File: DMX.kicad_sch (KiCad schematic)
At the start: 11 parts, among them J2 NC3FAAH, U2 CA-IS2092A

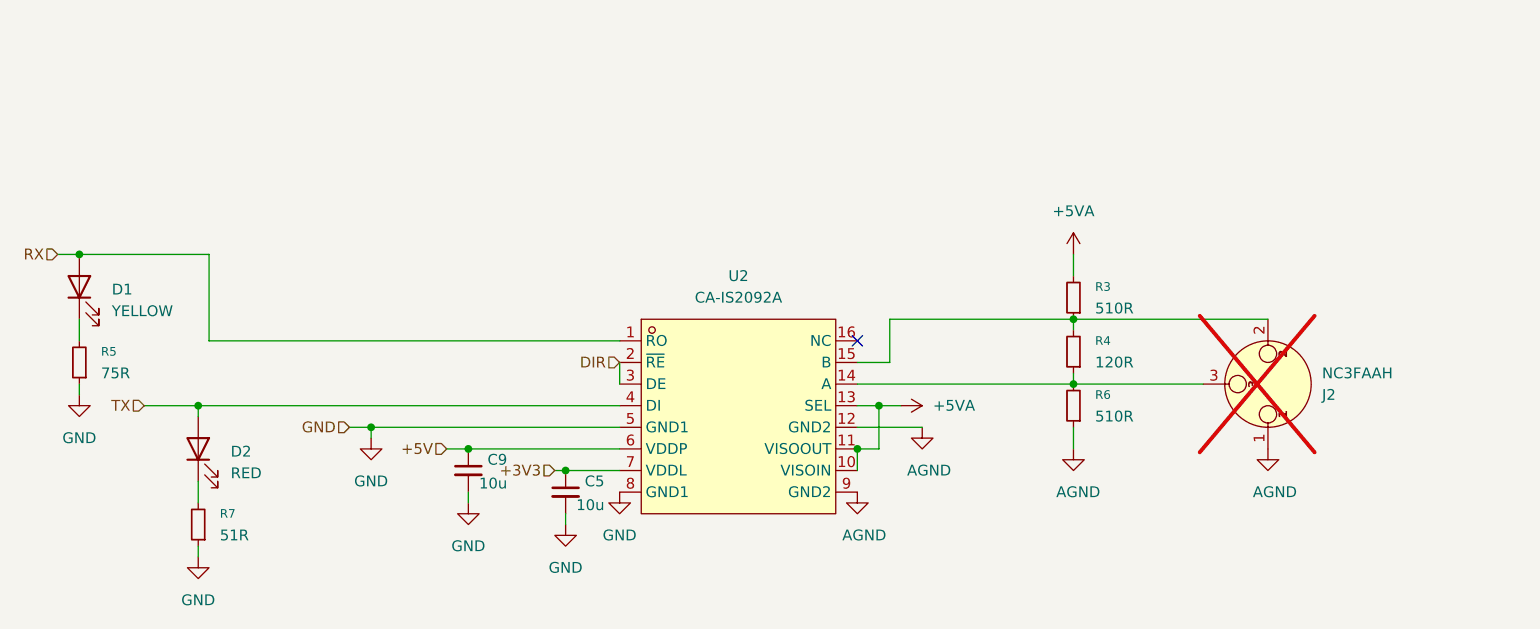
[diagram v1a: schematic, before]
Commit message: v0.2 new DMX circuitry
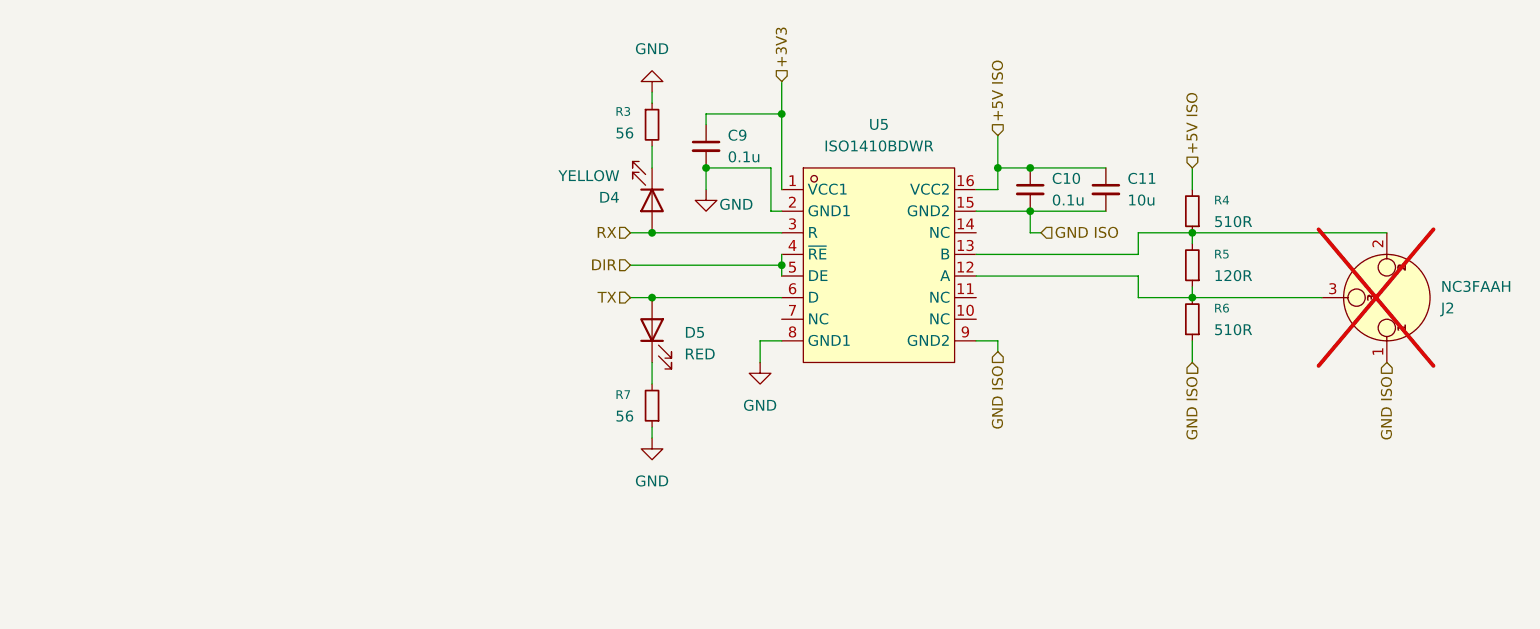
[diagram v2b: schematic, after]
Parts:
- removed C5: 10u, Capacitor_SMD:C_0603_1608Metric, symbol Device:C_Small
- removed D2: RED, LED_SMD:LED_0805_2012Metric, symbol Device:LED
- removed U2: CA-IS2092A, EasyEDA:LGA-16_L5.2-W4.7-P0.65-TL_CA-IS2062A-FRANK2, symbol IS2092A:CA-IS2092A
- added C10: 0.1u, Capacitor_SMD:C_0603_1608Metric, symbol Device:C_Small
- added C11: 10u, Capacitor_SMD:C_0603_1608Metric, symbol Device:C_Small
- added D5: RED, LED_SMD:LED_0805_2012Metric, symbol Device:LED
- added U5: ISO1410BDWR, EasyEDA:SOIC-16_L10.3-W7.5-P1.27-LS10.3-BL, symbol impart EasyEDA:ISO1410BDWR
- C9: value 10u -> 0.1u; LCSC Part C96446 -> C14663
- J2: LCSC Part (none) -> C368521
- R3: renamed from R5; value 75R -> 56
- R7: value 51R -> 56
- renumbered D1 to D4, R3 to R4, R4 to R5
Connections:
- net +5V is gone; now on net +3V3: C9.1
- net +3V3: now also U5.1 (VCC1)
- net DIR: now also U5.4 (~{RE}), U5.5 (DE)
- net GND: now also U5.2 (GND1), U5.8 (GND1)
- net RX: now also U5.3 (R)
- net TX: now also D5.2 (A), U5.6 (D)
- net at J2.2, R4.1, R5.2: now also U5.13 (B)
- net at J2.3, R5.1, R6.2: now also U5.12 (A)
- net at R7.2: now also D5.1 (K)
- net +5VA renamed +5V ISO
- net +5V ISO: now also C10.1, C11.1, U5.16 (VCC2)
- net AGND renamed GND ISO
- net GND ISO: now also C10.2, C11.2, U5.15 (GND2), U5.9 (GND2)
- no-connect marks 1 -> 0
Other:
- moved on the sheet: D4, J2, R3, R4, R5, R6

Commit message: change solder jumpers to pins & power break out
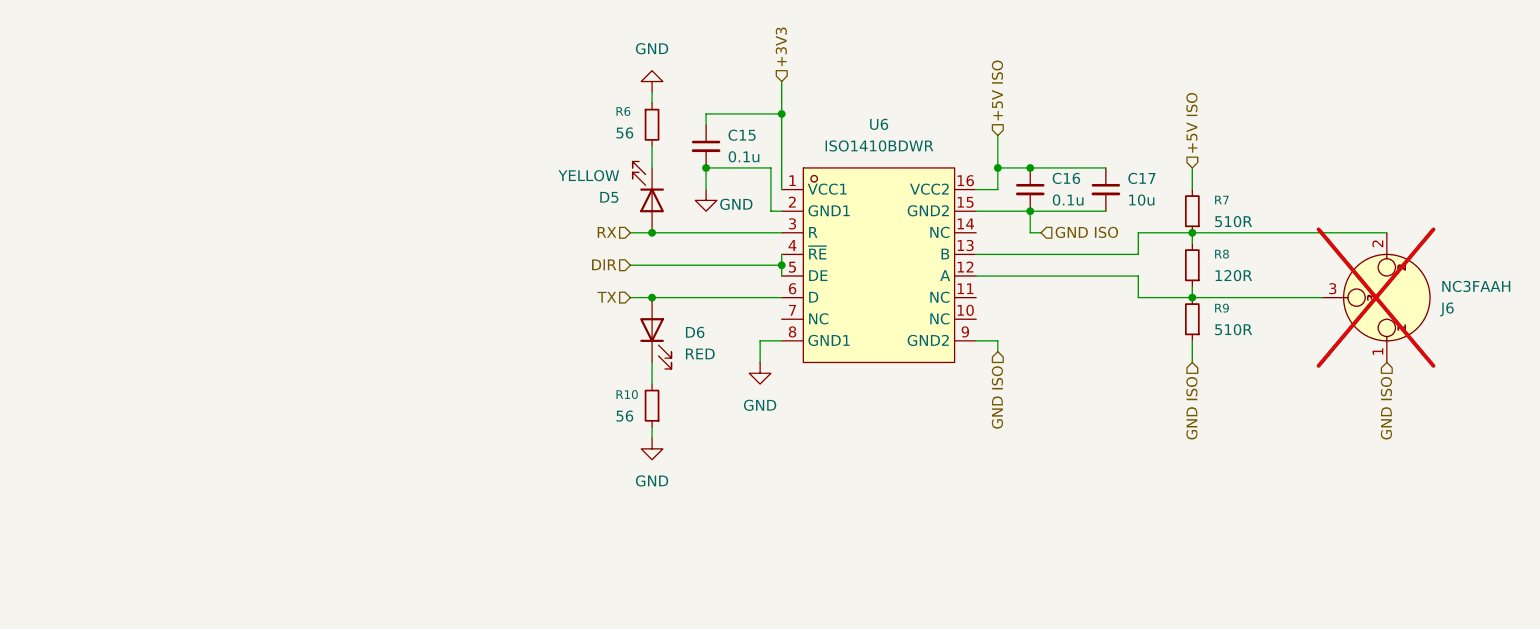
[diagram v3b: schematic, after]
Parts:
- renumbered C9 to C15, C10 to C16, C11 to C17, D4 to D5, D5 to D6, J2 to J6, R7 to R10, R3 to R6, R4 to R7, R5 to R8, R6 to R9, U5 to U6

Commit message: remove PoE Breakout & rund DRC
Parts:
- J6: footprint Connector_Audio:Jack_XLR_Neutrik_NC3FAAH_Horizontal -> Connector_Audio:Jack_XLR_Neutrik_NC3FAAH_Horizontal_Board-Overhang
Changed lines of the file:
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@@
 			)
 		)
-		(property "Footprint" "Connector_Audio:Jack_XLR_Neutrik_NC3FAAH_Horizontal"
+		(property "Footprint" "Connector_Audio:Jack_XLR_Neutrik_NC3FAAH_Horizontal_Board-Overhang"
 			(at 250.19 76.2 0)
 			(effects
